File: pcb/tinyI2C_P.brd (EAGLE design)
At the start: 83.2 x 83.2 mm, 226 parts, among them IC1 74ABT125BQ, IC10 74ABT125BQ, IC11 TPS76318, IC12 74ABT125BQ, IC13 TPS76318, IC14 74ABT125BQ, IC15 TPS76318, IC16 74ABT125BQ, IC2 TPS76318, IC3 TPS76318, IC4 74ABT125BQ, IC5 TPS76318, IC6 74ABT125BQ, IC7 TPS76318, IC8 74ABT125BQ, IC9 TPS76318, U1 LPC824M201JHI33, U2 LPC824M201JHI33, U3 LPC824M201JHI33, U4 LPC824M201JHI33, U5 LPC824M201JHI33, U6 LPC824M201JHI33, U7 LPC824M201JHI33, U8 LPC824M201JHI33, X1 TSW-112-02-S-S, X10 TSW-112-02-S-S, X11 TSW-112-02-S-S, X12 TSW-102-02-S-S, X13 TSW-106-02-S-S-RA, X14 TSW-112-02-S-S, X15 TSW-112-02-S-S, X16 TSW-102-02-S-S, X17 TSW-106-02-S-S-RA, X18 TSW-112-02-S-S, X19 TSW-112-02-S-S, X2 TSW-106-02-S-S-RA, X20 TSW-102-02-S-S, X21 TSW-106-02-S-S-RA, X22 TSW-112-02-S-S, X23 TSW-112-02-S-S, X24 TSW-102-02-S-S, X25 TSW-106-02-S-S-RA, X26 TSW-112-02-S-S, X27 TSW-112-02-S-S, X28 TSW-102-02-S-S, X29 TSW-106-02-S-S-RA, X3 TSW-112-02-S-S, X30 TSW-112-02-S-S, X31 TSW-112-02-S-S, X32 TSW-102-02-S-S, X4 TSW-102-02-S-S, X5 TSW-106-02-S-S-RA, X6 TSW-112-02-S-S, X7 TSW-112-02-S-S, X8 TSW-102-02-S-S, X9 TSW-106-02-S-S-RA

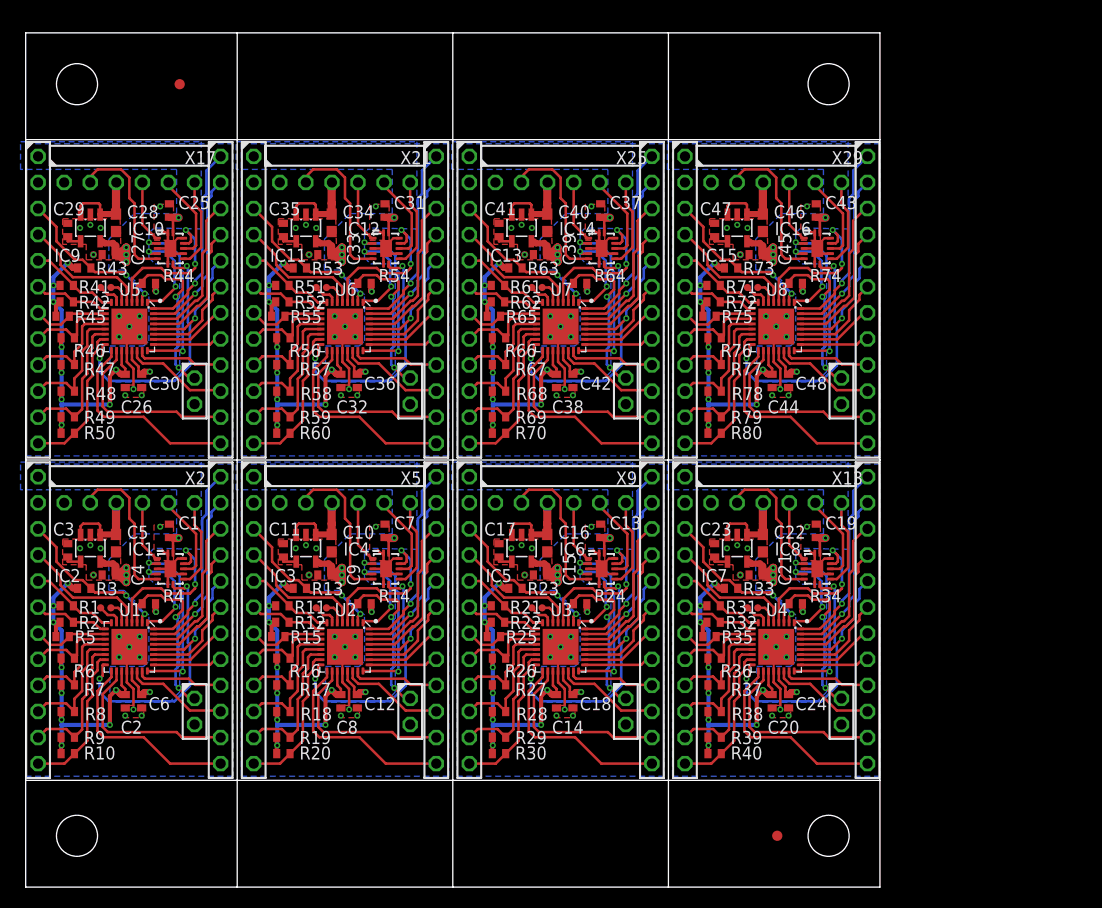
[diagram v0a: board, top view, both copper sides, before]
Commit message: [ PCB ] panelized as per update
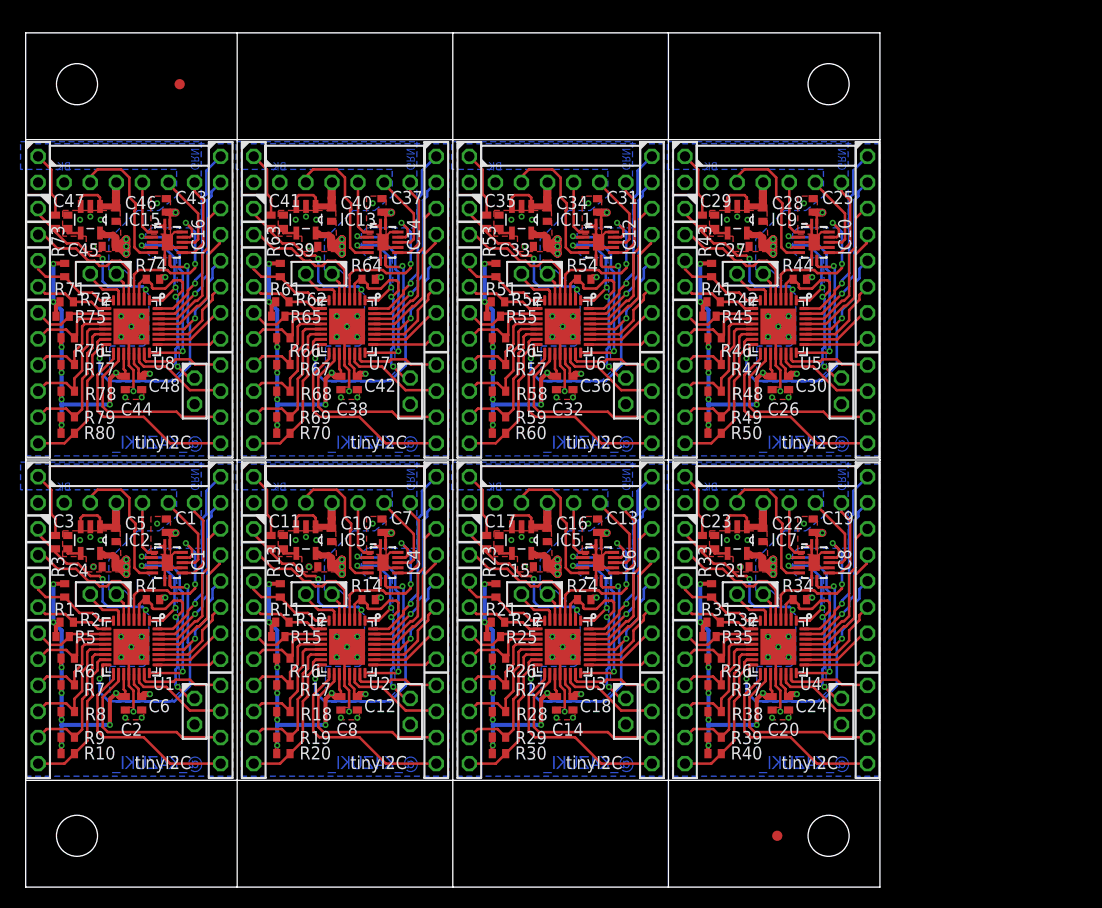
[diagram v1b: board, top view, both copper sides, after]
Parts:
- removed TP27, TP28, TP29, TP30, TP31, TP32, TP33, TP34, TP35, TP36, TP37, TP38, TP39, TP40, TP41, TP42: TPTP07R, testpad:TP07R
- added X33, X37, X38: TSW-112-02-S-S, con-samtec.local:TSW-112-02-S-S
- added X34, X35, X39, X40: TSW-102-02-S-S, con-samtec.local:TSW-102-02-S-S
- added X36: TSW-106-02-S-S-RA, con-samtec.local:TSW-106-02-S-S-RA
- C10, C16, C22, C28, C34, C40, C46, C5: device rcl:C1608 -> rcl:C0402
- IC1, IC10, IC12, IC14, IC16, IC4, IC6, IC8: value 74ABT125BQ -> IC_TTL_74_125; device 74xx-eu_local:DHVQFN14 -> mylib:DHVQFN14
- IC11, IC13, IC15, IC2, IC3, IC5, IC7, IC9: value TPS76318 -> TPS73618(0.4A); device texas:SOT23-DBV -> mylib:SOT95P280X145-5N
- U1, U2, U3, U4, U5, U6, U7, U8: device mbed-HDK:HVQFN33 -> mylib:HVQFN33
- X10, X14, X15, X19, X30: value TSW-112-02-S-S -> TSW-102-02-S-S; device con-samtec.local:TSW-112-02-S-S -> con-samtec.local:TSW-102-02-S-S
- X11, X26, X31, X6: value TSW-112-02-S-S -> TSW-106-02-S-S-RA; device con-samtec.local:TSW-112-02-S-S -> con-samtec.local:TSW-106-02-S-S-RA
- X12, X28, X32, X8: value TSW-102-02-S-S -> TSW-112-02-S-S; device con-samtec.local:TSW-102-02-S-S -> con-samtec.local:TSW-112-02-S-S
- X13, X17: value TSW-106-02-S-S-RA -> TSW-112-02-S-S; device con-samtec.local:TSW-106-02-S-S-RA -> con-samtec.local:TSW-112-02-S-S
- X16: value TSW-102-02-S-S -> TSW-106-02-S-S-RA; device con-samtec.local:TSW-102-02-S-S -> con-samtec.local:TSW-106-02-S-S-RA
- X25, X29, X5, X9: value TSW-106-02-S-S-RA -> TSW-102-02-S-S; device con-samtec.local:TSW-106-02-S-S-RA -> con-samtec.local:TSW-102-02-S-S
- moved X18 86.6 mm to (82.0, 26.0)
- moved X19 72.5 mm to (79.5, 17.1)
- moved X17 69.8 mm to (64.2, 26.0), turned to 90 degrees
- moved R73 66.0 mm to (2.90, 64.8), turned to 90 degrees
- moved R44 63.4 mm to (75.4, 59.2)
- moved IC16 63.3 mm to (13.8, 62.8)
- moved C43 63.3 mm to (13.7, 66.4)
- moved R71 63.2 mm to (3.80, 60.1), turned to 90 degrees
- moved U5 63.2 mm to (73.3, 54.6)
- moved C28 63.0 mm to (71.8, 65.5)
- moved C46 63.0 mm to (8.80, 65.5)
- moved IC15 63.0 mm to (6.30, 65.0), turned to 270 degrees
- moved IC9 63.0 mm to (69.3, 65.0), turned to 270 degrees
- moved C27 63.0 mm to (71.1, 62.4)
- moved C29 63.0 mm to (67.1, 64.8)
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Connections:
- net !ISP!1: now also X7.3; no longer X6.3
- net !ISP!2: now also X12.3; no longer X10.3
- net !ISP!3: now also X17.3; no longer X14.3
- net !ISP!4: now also X22.3; no longer X18.3
- net !ISP!5: now also X27.3; no longer X22.3
- net !ISP!6: now also X32.3; no longer X26.3
- net !ISP!7: now also X37.3; no longer X30.3
- net !RESET!1: now also X9.1; no longer X8.1
- net !RESET!2: now also X14.1; no longer X12.1
- net !RESET!3: now also X19.1; no longer X16.1
- net !RESET!4: now also X24.1; no longer X20.1
- net !RESET!5: now also X29.1; no longer X24.1
- net !RESET!6: now also X34.1; no longer X28.1
- net !RESET!7: now also X39.1; no longer X32.1
- net 1.8V1: now also X7.1; no longer X6.1
- net 1.8V2: now also TP10.TP, X12.1; no longer TP14.TP, X10.1
- net 1.8V3: now also TP13.TP, X17.1; no longer TP19.TP, X14.1
- net 1.8V4: now also TP16.TP, X22.1; no longer TP24.TP, X18.1
- net 1.8V5: now also TP19.TP, X27.1; no longer TP29.TP, X22.1
- net 1.8V6: now also TP22.TP, X32.1; no longer TP34.TP, X26.1
- net 1.8V7: now also TP25.TP, X37.1; no longer TP39.TP, X30.1
- net 5V1: now also X6.3; no longer X5.3
- net 5V2: now also TP9.TP, X11.3; no longer TP13.TP, X9.3
- net 5V3: now also TP12.TP, X16.3; no longer TP18.TP, X13.3
- net 5V4: now also TP15.TP, X21.3; no longer TP23.TP, X17.3
- net 5V5: now also TP18.TP, X26.3; no longer TP28.TP, X21.3
- net 5V6: now also TP21.TP, X31.3; no longer TP33.TP, X25.3
- net 5V7: now also TP24.TP, X36.3; no longer TP38.TP, X29.3
- net CTS<-1: now also X6.2; no longer X5.2
- net CTS<-2: now also X11.2; no longer X9.2
- net CTS<-3: now also X16.2; no longer X13.2
- net CTS<-4: now also X21.2; no longer X17.2
- net CTS<-5: now also X26.2; no longer X21.2
- net CTS<-6: now also X31.2; no longer X25.2
- net CTS<-7: now also X36.2; no longer X29.2
- net GND1: now also TP8.TP, X6.1, X7.2, X9.2; no longer TP12.TP, X5.1, X6.2, X8.2
- net GND2: now also TP11.TP, X11.1, X14.2; no longer TP17.TP, X10.2, X9.1
- net GND3: now also TP14.TP, X16.1, X17.2, X19.2; no longer TP22.TP, X13.1, X14.2, X16.2
- net GND4: now also TP17.TP, X21.1, X22.2, X24.2; no longer TP27.TP, X17.1, X18.2, X20.2
- net GND5: now also TP20.TP, X26.1, X27.2, X29.2; no longer TP32.TP, X21.1, X22.2, X24.2
- net GND6: now also TP23.TP, X31.1, X32.2, X34.2; no longer TP37.TP, X25.1, X26.2, X28.2
- net GND7: now also TP26.TP, X36.1, X37.2, X39.2; no longer TP42.TP, X29.1, X30.2, X32.2
- net GPIO08: now also X7.4; no longer X6.4
- net GPIO09: now also X7.7; no longer X6.7
- net GPIO100: now also X33.5; no longer X27.5
- net GPIO101: now also X33.4; no longer X27.4
- net GPIO102: now also X33.3; no longer X27.3
- net GPIO103: now also X33.2; no longer X27.2
- net GPIO104: now also X33.1; no longer X27.1
- net GPIO105: now also X37.4; no longer X30.4
- net GPIO106: now also X37.7; no longer X30.7
- net GPIO107: now also X37.8; no longer X30.8
- net GPIO108: now also X37.9; no longer X30.9
- net GPIO109: now also X37.10; no longer X30.10
- net GPIO110: now also X37.11; no longer X30.11
- net GPIO111: now also X37.12; no longer X30.12
- net GPIO112: now also X38.8; no longer X31.8
- net GPIO113: now also X38.7; no longer X31.7
- net GPIO114: now also X38.6; no longer X31.6
- net GPIO115: now also X38.5; no longer X31.5
- net GPIO116: now also X38.4; no longer X31.4
- net GPIO117: now also X38.3; no longer X31.3
- net GPIO118: now also X38.2; no longer X31.2
- net GPIO119: now also X38.1; no longer X31.1
- net GPIO17: now also X7.8; no longer X6.8
- net GPIO18: now also X7.9; no longer X6.9
- net GPIO19: now also X7.10; no longer X6.10
- net GPIO20: now also X7.11; no longer X6.11
- net GPIO21: now also X7.12; no longer X6.12
- net GPIO22: now also X8.8; no longer X7.8
- net GPIO23: now also X8.7; no longer X7.7
- net GPIO24: now also X8.6; no longer X7.6
- net GPIO25: now also X8.5; no longer X7.5
- net GPIO26: now also X8.4; no longer X7.4
- net GPIO27: now also X8.3; no longer X7.3
- net GPIO28: now also X8.2; no longer X7.2
- net GPIO29: now also X8.1; no longer X7.1
- net GPIO30: now also X12.4; no longer X10.4
- net GPIO31: now also X12.7; no longer X10.7
- net GPIO32: now also X12.8; no longer X10.8
- net GPIO33: now also X12.9; no longer X10.9
- net GPIO34: now also X12.10; no longer X10.10
- net GPIO35: now also X12.11; no longer X10.11
- net GPIO36: now also X12.12; no longer X10.12
- net GPIO37: now also X13.8; no longer X11.8
- net GPIO38: now also X13.7; no longer X11.7
- net GPIO39: now also X13.6; no longer X11.6
- net GPIO40: now also X13.5; no longer X11.5
- net GPIO41: now also X13.4; no longer X11.4
- net GPIO42: now also X13.3; no longer X11.3
- net GPIO43: now also X13.2; no longer X11.2
- net GPIO44: now also X13.1; no longer X11.1
- net GPIO45: now also X17.4; no longer X14.4
- net GPIO46: now also X17.7; no longer X14.7
- net GPIO47: now also X17.8; no longer X14.8
- net GPIO48: now also X17.9; no longer X14.9
- net GPIO49: now also X17.10; no longer X14.10
- net GPIO50: now also X17.11; no longer X14.11
- net GPIO51: now also X17.12; no longer X14.12
- net GPIO52: now also X18.8; no longer X15.8
- net GPIO53: now also X18.7; no longer X15.7
- net GPIO54: now also X18.6; no longer X15.6
- net GPIO55: now also X18.5; no longer X15.5
- net GPIO56: now also X18.4; no longer X15.4
- net GPIO57: now also X18.3; no longer X15.3
- net GPIO58: now also X18.2; no longer X15.2
- net GPIO59: now also X18.1; no longer X15.1
- net GPIO60: now also X22.4; no longer X18.4
- net GPIO61: now also X22.7; no longer X18.7
- net GPIO62: now also X22.8; no longer X18.8
- net GPIO63: now also X22.9; no longer X18.9
- net GPIO64: now also X22.10; no longer X18.10
- net GPIO65: now also X22.11; no longer X18.11
- net GPIO66: now also X22.12; no longer X18.12
- net GPIO67: now also X23.8; no longer X19.8
- net GPIO68: now also X23.7; no longer X19.7
- net GPIO69: now also X23.6; no longer X19.6
- net GPIO70: now also X23.5; no longer X19.5
- net GPIO71: now also X23.4; no longer X19.4
- net GPIO72: now also X23.3; no longer X19.3
- net GPIO73: now also X23.2; no longer X19.2
- net GPIO74: now also X23.1; no longer X19.1
- net GPIO75: now also X27.4; no longer X22.4
- net GPIO76: now also X27.7; no longer X22.7
- net GPIO77: now also X27.8; no longer X22.8
- net GPIO78: now also X27.9; no longer X22.9
- net GPIO79: now also X27.10; no longer X22.10
- net GPIO80: now also X27.11; no longer X22.11
- net GPIO81: now also X27.12; no longer X22.12
- net GPIO82: now also X28.8; no longer X23.8
- net GPIO83: now also X28.7; no longer X23.7
- net GPIO84: now also X28.6; no longer X23.6
- net GPIO85: now also X28.5; no longer X23.5
- net GPIO86: now also X28.4; no longer X23.4
- net GPIO87: now also X28.3; no longer X23.3
- net GPIO88: now also X28.2; no longer X23.2
- net GPIO89: now also X28.1; no longer X23.1
- net GPIO90: now also X32.4; no longer X26.4
- net GPIO91: now also X32.7; no longer X26.7
- net GPIO92: now also X32.8; no longer X26.8
- net GPIO93: now also X32.9; no longer X26.9
- net GPIO94: now also X32.10; no longer X26.10
- net GPIO95: now also X32.11; no longer X26.11
- net GPIO96: now also X32.12; no longer X26.12
- net GPIO97: now also X33.8; no longer X27.8
- net GPIO98: now also X33.7; no longer X27.7
- net GPIO99: now also X33.6; no longer X27.6
- net I2C_SCL1: now also X7.6; no longer X6.6
- net I2C_SCL2: now also X12.6; no longer X10.6
- net I2C_SCL3: now also X17.6; no longer X14.6
- net I2C_SCL4: now also X22.6; no longer X18.6
- net I2C_SCL5: now also X27.6; no longer X22.6
- net I2C_SCL6: now also X32.6; no longer X26.6
- net I2C_SCL7: now also X37.6; no longer X30.6
- net I2C_SDA1: now also X7.5; no longer X6.5
- net I2C_SDA2: now also X12.5; no longer X10.5
- net I2C_SDA3: now also X17.5; no longer X14.5
- net I2C_SDA4: now also X22.5; no longer X18.5
- net I2C_SDA5: now also X27.5; no longer X22.5
- net I2C_SDA6: now also X32.5; no longer X26.5
- net I2C_SDA7: now also X37.5; no longer X30.5
- net RTS->1: now also X6.6; no longer X5.6
- net RTS->2: now also X11.6; no longer X9.6
- net RTS->3: now also X16.6; no longer X13.6
- net RTS->4: now also X21.6; no longer X17.6
- net RTS->5: now also X26.6; no longer X21.6
- net RTS->6: now also X31.6; no longer X25.6
- net RTS->7: now also X36.6; no longer X29.6
- net RX<-1: now also X6.5; no longer X5.5
- net RX<-2: now also X11.5; no longer X9.5
- net RX<-3: now also X16.5; no longer X13.5
- net RX<-4: now also X21.5; no longer X17.5
- net RX<-5: now also X26.5; no longer X21.5
- net RX<-6: now also X31.5; no longer X25.5
- net RX<-7: now also X36.5; no longer X29.5
- net SPI_CS1: now also X8.12; no longer X7.12
- net SPI_CS2: now also X13.12; no longer X11.12
- net SPI_CS3: now also X18.12; no longer X15.12
- net SPI_CS4: now also X23.12; no longer X19.12
- net SPI_CS5: now also X28.12; no longer X23.12
- net SPI_CS6: now also X33.12; no longer X27.12
- net SPI_CS7: now also X38.12; no longer X31.12
- net SPI_MISO1: now also X8.10; no longer X7.10
- net SPI_MISO2: now also X13.10; no longer X11.10
- net SPI_MISO3: now also X18.10; no longer X15.10
- net SPI_MISO4: now also X23.10; no longer X19.10
- net SPI_MISO5: now also X28.10; no longer X23.10
- net SPI_MISO6: now also X33.10; no longer X27.10
- net SPI_MISO7: now also X38.10; no longer X31.10
- net SPI_MOSI1: now also X8.9; no longer X7.9
- net SPI_MOSI2: now also X13.9; no longer X11.9
- net SPI_MOSI3: now also X18.9; no longer X15.9
- net SPI_MOSI4: now also X23.9; no longer X19.9
- net SPI_MOSI5: now also X28.9; no longer X23.9
- net SPI_MOSI6: now also X33.9; no longer X27.9
- net SPI_MOSI7: now also X38.9; no longer X31.9
- net SPI_SCK1: now also X8.11; no longer X7.11
- net SPI_SCK2: now also X13.11; no longer X11.11
- net SPI_SCK3: now also X18.11; no longer X15.11
- net SPI_SCK4: now also X23.11; no longer X19.11
- net SPI_SCK5: now also X28.11; no longer X23.11
- net SPI_SCK6: now also X33.11; no longer X27.11
- net SPI_SCK7: now also X38.11; no longer X31.11
- net SWCLK: now also X5.1; no longer TP8.TP
- net SWCLK1: now also X10.1; no longer TP10.TP
- net SWCLK2: now also X15.1; no longer TP15.TP
- net SWCLK3: now also X20.1; no longer TP20.TP
- net SWCLK4: now also X25.1; no longer TP25.TP
- net SWCLK5: now also X30.1; no longer TP30.TP
- net SWCLK6: now also X35.1; no longer TP35.TP
- net SWCLK7: now also X40.1; no longer TP40.TP
- net SWDIO: now also X5.2; no longer TP9.TP
- net SWDIO1: now also X10.2; no longer TP11.TP
- net SWDIO2: now also X15.2; no longer TP16.TP
- net SWDIO3: now also X20.2; no longer TP21.TP
- net SWDIO4: now also X25.2; no longer TP26.TP
- net SWDIO5: now also X30.2; no longer TP31.TP
- net SWDIO6: now also X35.2; no longer TP36.TP
- net SWDIO7: now also X40.2; no longer TP41.TP
- net TX->1: now also X6.4; no longer X5.4
- net TX->2: now also X11.4; no longer X9.4
- net TX->3: now also X16.4; no longer X13.4
- net TX->4: now also X21.4; no longer X17.4
- net TX->5: now also X26.4; no longer X21.4
- net TX->6: now also X31.4; no longer X25.4
- net TX->7: now also X36.4; no longer X29.4
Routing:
- net 1.8V6: track 50.1 -> 53.9 mm, vias 15 -> 14
- net 1.8V7: track 50.1 -> 53.9 mm, vias 15 -> 14
- net 1.8V5: track 50.1 -> 53.9 mm, vias 15 -> 14
- net 1.8V4: track 50.1 -> 53.9 mm, vias 15 -> 14
- net 1.8V2: track 50.1 -> 53.9 mm, vias 15 -> 14
- net 1.8V3: track 50.1 -> 53.9 mm, vias 15 -> 14
- net 1.8V: track 50.1 -> 53.9 mm, vias 15 -> 14
- net 1.8V1: track 50.1 -> 53.9 mm, vias 15 -> 14
- net SWDIO7: track 2.44 -> 4.45 mm
- net SWDIO6: track 2.44 -> 4.45 mm
- net SWDIO5: track 2.44 -> 4.45 mm
- net SWDIO4: track 2.44 -> 4.45 mm
- net SWDIO: track 2.44 -> 4.45 mm
- net SWDIO1: track 2.44 -> 4.45 mm
- net SWDIO3: track 2.44 -> 4.45 mm
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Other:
- board text added: "@_K4ZUKI_"
- board text added: "BK"
- board text added: "GRN"
- board text added: "tinyI2C"
- board text removed: "X2"

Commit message: [ PCB ] trace change and panelize
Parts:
- moved R16 0.50 mm to (24.6, 22.3)
- moved R17 0.50 mm to (24.6, 19.7)
- moved R18 0.50 mm to (24.6, 17.1)
- moved R19 0.50 mm to (24.6, 14.6)
- moved R26 0.50 mm to (45.6, 22.3)
- moved R27 0.50 mm to (45.6, 19.7)
- moved R28 0.50 mm to (45.6, 17.1)
- moved R29 0.50 mm to (45.6, 14.6)
- moved R36 0.50 mm to (66.6, 22.3)
- moved R37 0.50 mm to (66.6, 19.7)
- moved R38 0.50 mm to (66.6, 17.1)
- moved R39 0.50 mm to (66.6, 14.6)
- moved R46 0.50 mm to (66.6, 53.5)
- moved R47 0.50 mm to (66.6, 50.9)
- moved R48 0.50 mm to (66.6, 48.3)
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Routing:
- net 1.8V7: track 53.9 -> 54.7 mm
- net 1.8V6: track 53.9 -> 54.7 mm
- net 1.8V4: track 53.9 -> 54.7 mm
- net 1.8V5: track 53.9 -> 54.7 mm
- net 1.8V3: track 53.9 -> 54.7 mm
- net 1.8V2: track 53.9 -> 54.7 mm
- net 1.8V1: track 53.9 -> 54.7 mm
- net 1.8V: track 53.9 -> 54.7 mm

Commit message: [ PCB ] panelized based on sch/brd updates
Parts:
- added C49, C50, C51, C52, C53, C54, C55, C56, C57, C58, C59, C60, C61, C62, C63, C64, C65, C66, C67, C68, C69, C70, C71, C72: 1005, mylib:C0402
- added IC17, IC19, IC20, IC22, IC23: 74LVC1G125DCK, 74xx-little-us_local:SC70-5
- added IC18, IC21, IC24: IC_LDO_MIC5355, mylib:IC_08_0.65_160MIL
- added Q1, Q2, Q3, Q4, Q5, Q6, Q7, Q8: (no value), adafruit (1):NX3225
- added TP27, TP28, TP29, TP30, TP31, TP32, TP33, TP34: TPTP07R, testpad_local:TP07R
- added X41, X42, X46, X47, X48: TSW-102-02-S-S, con-samtec.local:TSW-102-02-S-S
- added X43: TSW-106-02-S-S-RA, con-samtec.local:TSW-106-02-S-S-RA
- added X44, X45: TSW-112-02-S-S, con-samtec.local:TSW-112-02-S-S
- C1, C11, C12, C13, C14, C15, C17, C18, C19, C2, C20, C21, C23, C24, C25, C26, C27, C29, C3, C30, C31, C32, C33, C35, C36, C37, C38, C39, C4, C41, C42, C43, C44, C45, C47, C48, C6, C7, C8, C9: device rcl:C1005 -> mylib:C0402
- C10, C16, C22, C28, C34, C40, C46, C5: value 1608 -> 1005; device rcl:C0402 -> mylib:C0402
- IC1, IC10, IC14, IC16, IC4, IC8: value IC_TTL_74_125 -> 74LVC1G125DCK; device mylib:DHVQFN14 -> 74xx-little-us_local:SC70-5
- IC11, IC13, IC2, IC5, IC7: value TPS73618(0.4A) -> 74LVC1G125DCK; device mylib:SOT95P280X145-5N -> 74xx-little-us_local:SC70-5
- IC12, IC6: value IC_TTL_74_125 -> IC_LDO_MIC5355; device mylib:DHVQFN14 -> mylib:IC_08_0.65_160MIL
- IC15, IC3, IC9: value TPS73618(0.4A) -> IC_LDO_MIC5355; device mylib:SOT95P280X145-5N -> mylib:IC_08_0.65_160MIL
- R1, R10, R11, R12, R13, R14, R15, R16, R17, R18, R19, R2, R20, R21, R22, R23, R24, R25, R26, R27, R28, R29, R3, R30, R31, R32, R33, R34, R35, R36, R37, R38, R39, R4, R40, R41, R42, R43, R44, R45, R46, R47, R48, R49, R5, R50, R51, R52, R53, R54, R55, R56, R57, R58, R59, R6, R60, R61, R62, R63, R64, R65, R66, R67, R68, R69, R7, R70, R71, R72, R73, R74, R75, R76, R77, R78, R79, R8, R80, R9: device rcl:R1005 -> mylib:C0402
- TP1, TP10, TP11, TP12, TP13, TP14, TP15, TP16, TP17, TP18, TP19, TP2, TP20, TP21, TP22, TP23, TP24, TP25, TP26, TP3, TP6, TP7, TP8, TP9: device testpad:TP07R -> testpad_local:TP07R
- X11, X16, X36, X6: value TSW-106-02-S-S-RA -> TSW-102-02-S-S; device con-samtec.local:TSW-106-02-S-S-RA -> con-samtec.local:TSW-102-02-S-S
- X12, X17, X18, X22, X23, X28: value TSW-112-02-S-S -> TSW-102-02-S-S; device con-samtec.local:TSW-112-02-S-S -> con-samtec.local:TSW-102-02-S-S
- X13, X3, X37, X7: value TSW-112-02-S-S -> TSW-106-02-S-S-RA; device con-samtec.local:TSW-112-02-S-S -> con-samtec.local:TSW-106-02-S-S-RA
- X14, X15, X20, X39, X9: value TSW-102-02-S-S -> TSW-112-02-S-S; device con-samtec.local:TSW-102-02-S-S -> con-samtec.local:TSW-112-02-S-S
- X19, X25: value TSW-102-02-S-S -> TSW-106-02-S-S-RA; device con-samtec.local:TSW-102-02-S-S -> con-samtec.local:TSW-106-02-S-S-RA
- X2, X21, X26: value TSW-106-02-S-S-RA -> TSW-112-02-S-S; device con-samtec.local:TSW-106-02-S-S-RA -> con-samtec.local:TSW-112-02-S-S
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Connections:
- removed net CTS<-: IC1.6, X2.2
- removed net CTS<-1: IC4.6, X6.2
- removed net CTS<-2: IC6.6, X11.2
- removed net CTS<-3: IC8.6, X16.2
- removed net CTS<-4: IC10.6, X21.2
- removed net CTS<-5: IC12.6, X26.2
- removed net CTS<-6: IC14.6, X31.2
- removed net CTS<-7: IC16.6, X36.2
- removed net RTS->: IC1.9, X2.6
- removed net RTS->1: IC4.9, X6.6
- removed net RTS->2: IC6.9, X11.6
- removed net RTS->3: IC8.9, X16.6
- removed net RTS->4: IC10.9, X21.6
- removed net RTS->5: IC12.9, X26.6
- removed net RTS->6: IC14.9, X31.6
- removed net RTS->7: IC16.9, X36.6
- removed net TGT_CTS: IC1.8, U1.16
- removed net TGT_CTS1: IC4.8, U2.16
- removed net TGT_CTS2: IC6.8, U3.16
- removed net TGT_CTS3: IC8.8, U4.16
- removed net TGT_CTS4: IC10.8, U5.16
- removed net TGT_CTS5: IC12.8, U6.16
- removed net TGT_CTS6: IC14.8, U7.16
- removed net TGT_CTS7: IC16.8, U8.16
- removed net TGT_RTS: IC1.5, U1.1
- removed net TGT_RTS1: IC4.5, U2.1
- removed net TGT_RTS2: IC6.5, U3.1
- removed net TGT_RTS3: IC8.5, U4.1
- removed net TGT_RTS4: IC10.5, U5.1
- removed net TGT_RTS5: IC12.5, U6.1
- removed net TGT_RTS6: IC14.5, U7.1
- removed net TGT_RTS7: IC16.5, U8.1
- new net 3.3V: C3.1, C7.1, IC1.5, IC3.8, TP6.TP
- new net 3.3V1: C14.1, C16.1, IC4.5, IC6.8, TP10.TP
- new net 3.3V2: C23.1, C25.1, IC7.5, IC9.8, TP14.TP
- new net 3.3V3: C32.1, C34.1, IC10.5, IC12.8, TP18.TP
- new net 3.3V4: C41.1, C43.1, IC13.5, IC15.8, TP22.TP
- new net 3.3V5: C50.1, C52.1, IC16.5, IC18.8, TP26.TP
- new net 3.3V6: C59.1, C61.1, IC19.5, IC21.8, TP30.TP
- new net 3.3V7: C68.1, C70.1, IC22.5, IC24.8, TP34.TP
- new net N$10: C45.1, Q5.3, U5.18
- new net N$11: C53.1, Q6.1, U6.17
- new net N$12: C54.1, Q6.3, U6.18
- new net N$13: C62.1, Q7.1, U7.17
- new net N$14: C63.1, Q7.3, U7.18
- new net N$15: C71.1, Q8.1, U8.17
- new net N$16: C72.1, Q8.3, U8.18
- new net N$9: C44.1, Q5.1, U5.17
- net !ISP!: now also X6.1; no longer X1.3
- net !ISP!1: now also X12.1; no longer X7.3
- net !ISP!2: now also X18.1; no longer X12.3
- net !ISP!3: now also X24.1; no longer X17.3
- net !ISP!4: now also X30.1; no longer X22.3
- net !ISP!5: now also X36.1; no longer X27.3
- net !ISP!6: now also X42.1; no longer X32.3
- net !ISP!7: now also X48.1; no longer X37.3
- net !RESET!1: now also X10.1; no longer X9.1
- net !RESET!2: now also X16.1; no longer X14.1
- net !RESET!3: now also X22.1; no longer X19.1
- net !RESET!4: now also X28.1; no longer X24.1
- net !RESET!5: now also X34.1; no longer X29.1
- net !RESET!6: now also X40.1; no longer X34.1
- net !RESET!7: now also X46.1; no longer X39.1
- net 1.8V: now also IC3.7; no longer IC1.14
- net 1.8V1: now also C10.1, C11.1, C15.1, IC5.5, IC6.7, TP8.TP, X8.1; no longer C7.1, C8.1, C9.1, IC3.5, IC4.14, TP7.TP, X7.1
- net 1.8V2: now also C19.1, C20.1, C21.1, C24.1, IC8.5, IC9.7, TP12.TP, X14.1; no longer C13.1, C14.1, C15.1, C18.1, IC5.5, IC6.14, TP10.TP, X12.1
- net 1.8V3: now also C28.1, C29.1, C30.1, C33.1, IC11.5, IC12.7, TP16.TP, X20.1; no longer C19.1, C20.1, C21.1, C24.1, IC7.5, IC8.14, TP13.TP, X17.1
- net 1.8V4: now also C37.1, C38.1, C39.1, C42.1, IC14.5, IC15.7, TP20.TP, X26.1; no longer C25.1, C26.1, C27.1, C30.1, IC10.14, IC9.5, TP16.TP, X22.1
- net 1.8V5: now also C46.1, C47.1, C48.1, C51.1, IC17.5, IC18.7, TP24.TP, X32.1; no longer C31.1, C32.1, C33.1, C36.1, IC11.5, IC12.14, TP19.TP, X27.1
- net 1.8V6: now also C55.1, C56.1, C57.1, C60.1, IC20.5, IC21.7, TP28.TP, X38.1; no longer C37.1, C38.1, C39.1, C42.1, IC13.5, IC14.14, TP22.TP, X32.1
- net 1.8V7: now also C64.1, C65.1, C66.1, C69.1, IC23.5, IC24.7, TP32.TP, X44.1; no longer C43.1, C44.1, C45.1, C48.1, IC15.5, IC16.14, TP25.TP, X37.1
- net 5V: now also IC3.1, IC3.4, IC3.5, X1.3, X3.3; no longer IC2.1, IC2.3, X2.3
- net 5V1: now also C13.1, IC6.1, IC6.4, IC6.5, TP7.TP, X7.3, X8.3; no longer C10.1, IC3.1, IC3.3, TP6.TP, X6.3
- net 5V2: now also C22.1, IC9.1, IC9.4, IC9.5, TP11.TP, X13.3, X14.3; no longer C16.1, IC5.1, IC5.3, TP9.TP, X11.3
- net 5V3: now also C31.1, IC12.1, IC12.4, IC12.5, TP15.TP, X19.3, X20.3; no longer C22.1, IC7.1, IC7.3, TP12.TP, X16.3
- net 5V4: now also C40.1, IC15.1, IC15.4, IC15.5, TP19.TP, X25.3, X26.3; no longer C28.1, IC9.1, IC9.3, TP15.TP, X21.3
- net 5V5: now also C49.1, IC18.1, IC18.4, IC18.5, TP23.TP, X31.3, X32.3; no longer C34.1, IC11.1, IC11.3, TP18.TP, X26.3
- net 5V6: now also C58.1, IC21.1, IC21.4, IC21.5, TP27.TP, X37.3, X38.3; no longer C40.1, IC13.1, IC13.3, TP21.TP, X31.3
- net 5V7: now also C67.1, IC24.1, IC24.4, IC24.5, TP31.TP, X43.3, X44.3; no longer C46.1, IC15.1, IC15.3, TP24.TP, X36.3
- net GND: now also C7.2, C8.2, C9.2, IC1.3, IC2.1, IC2.3, IC3.2, IC3.EXP, Q1.2, Q1.4, X3.1, X6.2; no longer IC1.10, IC1.13, IC1.4, IC1.7, IC1.EXP, IC2.2, X2.1
- net GND1: now also C13.2, C14.2, C15.2, C16.2, C17.2, C18.2, IC4.3, IC5.1, IC5.3, IC6.2, IC6.EXP, Q2.2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; no longer C7.2, C8.2, C9.2, IC3.2, IC4.10, IC4.13, IC4.4, IC4.7, IC4.EXP, TP8.TP, X6.1, X7.2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
- net GND2: now also C19.2, C20.2, C21.2, C22.2, C23.2, C24.2, C25.2, C26.2, C27.2, IC7.1, IC7.3, IC8.1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; no longer C13.2, C14.2, C15.2, C16.2, C17.2, C18.2, IC5.2, IC6.1, IC6.10, IC6.13, IC6.4, IC6.7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
- net GND3: now also C28.2, C29.2, C30.2, C31.2, C32.2, C33.2, C34.2, C35.2, C36.2, IC10.1, IC10.3, IC11.1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; no longer C19.2, C20.2, C21.2, C22.2, C23.2, C24.2, IC7.2, IC8.1, IC8.10, IC8.13, IC8.4, IC8.7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
- net GND4: now also C37.2, C38.2, C39.2, C40.2, C41.2, C42.2, C43.2, C44.2, C45.2, IC13.1, IC13.3, IC14.1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; no longer C25.2, C26.2, C27.2, C28.2, C29.2, C30.2, IC10.1, IC10.10, IC10.13, IC10.4, IC10.7, IC10.EXP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
- net GND5: now also C46.2, C47.2, C48.2, C49.2, C50.2, C51.2, C52.2, C53.2, C54.2, IC16.1, IC16.3, IC17.1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; no longer C31.2, C32.2, C33.2, C34.2, C35.2, C36.2, IC11.2, IC12.1, IC12.10, IC12.13, IC12.4, IC12.7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
- net GND6: now also C55.2, C56.2, C57.2, C58.2, C59.2, C60.2, C61.2, C62.2, C63.2, IC19.1, IC19.3, IC20.1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; no longer C37.2, C38.2, C39.2, C40.2, C41.2, C42.2, IC13.2, IC14.1, IC14.10, IC14.13, IC14.4, IC14.7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
- net GND7: now also C64.2, C65.2, C66.2, C67.2, C68.2, C69.2, C70.2, C71.2, C72.2, IC22.1, IC22.3, IC23.1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; no longer C43.2, C44.2, C45.2, C46.2, C47.2, C48.2, IC15.2, IC16.1, IC16.10, IC16.13, IC16.4, IC16.7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
- net GPIO00: now also X2.1; no longer X3.1
- net GPIO01: now also X2.2; no longer X3.2
- net GPIO02: now also X2.3; no longer X3.3
- net GPIO03: now also X2.4; no longer X3.4
- net GPIO04: now also X2.5; no longer X3.5
- net GPIO05: now also X2.6; no longer X3.6
- net GPIO06: now also X2.7; no longer X3.7
- net GPIO07: now also X2.8; no longer X3.8
- net GPIO08: now also X8.4; no longer X7.4
- net GPIO09: now also X8.7; no longer X7.7
- net GPIO100: now also X39.5; no longer X33.5
- net GPIO101: now also X39.4; no longer X33.4
- net GPIO102: now also X39.3; no longer X33.3
- net GPIO103: now also X39.2; no longer X33.2
- net GPIO104: now also X39.1; no longer X33.1
- net GPIO105: now also X44.4; no longer X37.4
- net GPIO106: now also X44.7; no longer X37.7
- net GPIO107: now also X44.8; no longer X37.8
- net GPIO108: now also X44.9; no longer X37.9
- net GPIO109: now also X44.10; no longer X37.10
- net GPIO110: now also X44.11; no longer X37.11
- net GPIO111: now also X44.12; no longer X37.12
- net GPIO112: now also X45.8; no longer X38.8
- net GPIO113: now also X45.7; no longer X38.7
- net GPIO114: now also X45.6; no longer X38.6
- net GPIO115: now also X45.5; no longer X38.5
- net GPIO116: now also X45.4; no longer X38.4
- net GPIO117: now also X45.3; no longer X38.3
- net GPIO118: now also X45.2; no longer X38.2
- net GPIO119: now also X45.1; no longer X38.1
- net GPIO17: now also X8.8; no longer X7.8
- net GPIO18: now also X8.9; no longer X7.9
- net GPIO19: now also X8.10; no longer X7.10
- net GPIO20: now also X8.11; no longer X7.11
- net GPIO21: now also X8.12; no longer X7.12
- net GPIO22: now also X9.8; no longer X8.8
- net GPIO23: now also X9.7; no longer X8.7
- net GPIO24: now also X9.6; no longer X8.6
- net GPIO25: now also X9.5; no longer X8.5
- net GPIO26: now also X9.4; no longer X8.4
- net GPIO27: now also X9.3; no longer X8.3
- net GPIO28: now also X9.2; no longer X8.2
- net GPIO29: now also X9.1; no longer X8.1
- net GPIO30: now also X14.4; no longer X12.4
- net GPIO31: now also X14.7; no longer X12.7
- net GPIO32: now also X14.8; no longer X12.8
- net GPIO33: now also X14.9; no longer X12.9
- net GPIO34: now also X14.10; no longer X12.10
- net GPIO35: now also X14.11; no longer X12.11
- net GPIO36: now also X14.12; no longer X12.12
- net GPIO37: now also X15.8; no longer X13.8
- net GPIO38: now also X15.7; no longer X13.7
- net GPIO39: now also X15.6; no longer X13.6
- net GPIO40: now also X15.5; no longer X13.5
- net GPIO41: now also X15.4; no longer X13.4
- net GPIO42: now also X15.3; no longer X13.3
- net GPIO43: now also X15.2; no longer X13.2
- net GPIO44: now also X15.1; no longer X13.1
- net GPIO45: now also X20.4; no longer X17.4
- net GPIO46: now also X20.7; no longer X17.7
- net GPIO47: now also X20.8; no longer X17.8
- net GPIO48: now also X20.9; no longer X17.9
- net GPIO49: now also X20.10; no longer X17.10
- net GPIO50: now also X20.11; no longer X17.11
- net GPIO51: now also X20.12; no longer X17.12
- net GPIO52: now also X21.8; no longer X18.8
- net GPIO53: now also X21.7; no longer X18.7
- net GPIO54: now also X21.6; no longer X18.6
- net GPIO55: now also X21.5; no longer X18.5
- net GPIO56: now also X21.4; no longer X18.4
- net GPIO57: now also X21.3; no longer X18.3
- net GPIO58: now also X21.2; no longer X18.2
- net GPIO59: now also X21.1; no longer X18.1
- net GPIO60: now also X26.4; no longer X22.4
- net GPIO61: now also X26.7; no longer X22.7
- net GPIO62: now also X26.8; no longer X22.8
- net GPIO63: now also X26.9; no longer X22.9
- net GPIO64: now also X26.10; no longer X22.10
- net GPIO65: now also X26.11; no longer X22.11
- net GPIO66: now also X26.12; no longer X22.12
- net GPIO67: now also X27.8; no longer X23.8
- net GPIO68: now also X27.7; no longer X23.7
- net GPIO69: now also X27.6; no longer X23.6
- net GPIO70: now also X27.5; no longer X23.5
- net GPIO71: now also X27.4; no longer X23.4
- net GPIO72: now also X27.3; no longer X23.3
- net GPIO73: now also X27.2; no longer X23.2
- net GPIO74: now also X27.1; no longer X23.1
- net GPIO75: now also X32.4; no longer X27.4
- net GPIO76: now also X32.7; no longer X27.7
- net GPIO77: now also X32.8; no longer X27.8
- net GPIO78: now also X32.9; no longer X27.9
- net GPIO79: now also X32.10; no longer X27.10
- net GPIO80: now also X32.11; no longer X27.11
- net GPIO81: now also X32.12; no longer X27.12
- net GPIO82: now also X33.8; no longer X28.8
- net GPIO83: now also X33.7; no longer X28.7
- net GPIO84: now also X33.6; no longer X28.6
- net GPIO85: now also X33.5; no longer X28.5
- net GPIO86: now also X33.4; no longer X28.4
- net GPIO87: now also X33.3; no longer X28.3
- net GPIO88: now also X33.2; no longer X28.2
- net GPIO89: now also X33.1; no longer X28.1
- net GPIO90: now also X38.4; no longer X32.4
- net GPIO91: now also X38.7; no longer X32.7
- net GPIO92: now also X38.8; no longer X32.8
- net GPIO93: now also X38.9; no longer X32.9
- net GPIO94: now also X38.10; no longer X32.10
- net GPIO95: now also X38.11; no longer X32.11
- net GPIO96: now also X38.12; no longer X32.12
- net GPIO97: now also X39.8; no longer X33.8
- net GPIO98: now also X39.7; no longer X33.7
- net GPIO99: now also X39.6; no longer X33.6
- net I2C_SCL1: now also X8.6; no longer X7.6
- net I2C_SCL2: now also X14.6; no longer X12.6
- net I2C_SCL3: now also X20.6; no longer X17.6
- net I2C_SCL4: now also X26.6; no longer X22.6
- net I2C_SCL5: now also X32.6; no longer X27.6
- net I2C_SCL6: now also X38.6; no longer X32.6
- net I2C_SCL7: now also X44.6; no longer X37.6
- net I2C_SDA1: now also X8.5; no longer X7.5
- net I2C_SDA2: now also X14.5; no longer X12.5
- net I2C_SDA3: now also X20.5; no longer X17.5
- net I2C_SDA4: now also X26.5; no longer X22.5
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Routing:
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- added copper zone on layer 1, net 1.8V
- added copper zone on layer 1, net 1.8V1
- added copper zone on layer 1, net 1.8V2
- added copper zone on layer 1, net 1.8V3
- added copper zone on layer 1, net 1.8V4
- added copper zone on layer 1, net 1.8V5
- added copper zone on layer 1, net 1.8V6
- added copper zone on layer 1, net 1.8V7
- added copper zone on layer 1, net 3.3V
- added copper zone on layer 1, net 3.3V1
- added copper zone on layer 1, net 3.3V2
- added copper zone on layer 1, net 3.3V3
- added copper zone on layer 1, net 3.3V4
- added copper zone on layer 1, net 3.3V5
- added copper zone on layer 1, net 3.3V6
- added copper zone on layer 1, net 3.3V7
- added copper zone on layer 1, net 5V
- added copper zone on layer 1, net 5V1
- added copper zone on layer 1, net 5V2
- added copper zone on layer 1, net 5V3
- added copper zone on layer 1, net 5V4
- added copper zone on layer 1, net 5V5
- added copper zone on layer 1, net 5V6
- added copper zone on layer 1, net 5V7
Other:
- board text added: "!ISP"
- board text added: "!RST"
- board text added: "C7"
- board text added: "C8"
- board text added: "C9"
- board text added: "IC3"

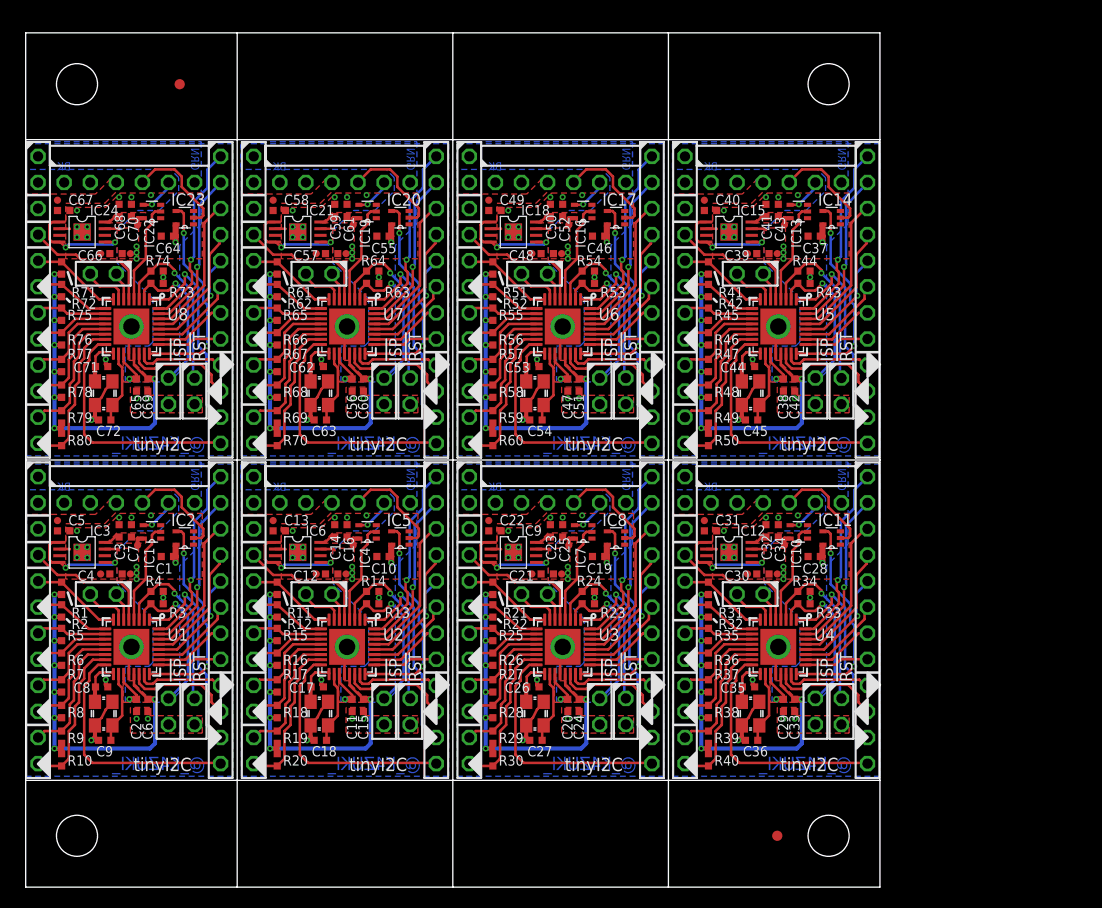
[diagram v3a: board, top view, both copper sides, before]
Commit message: [ PCB ] panelize as updated
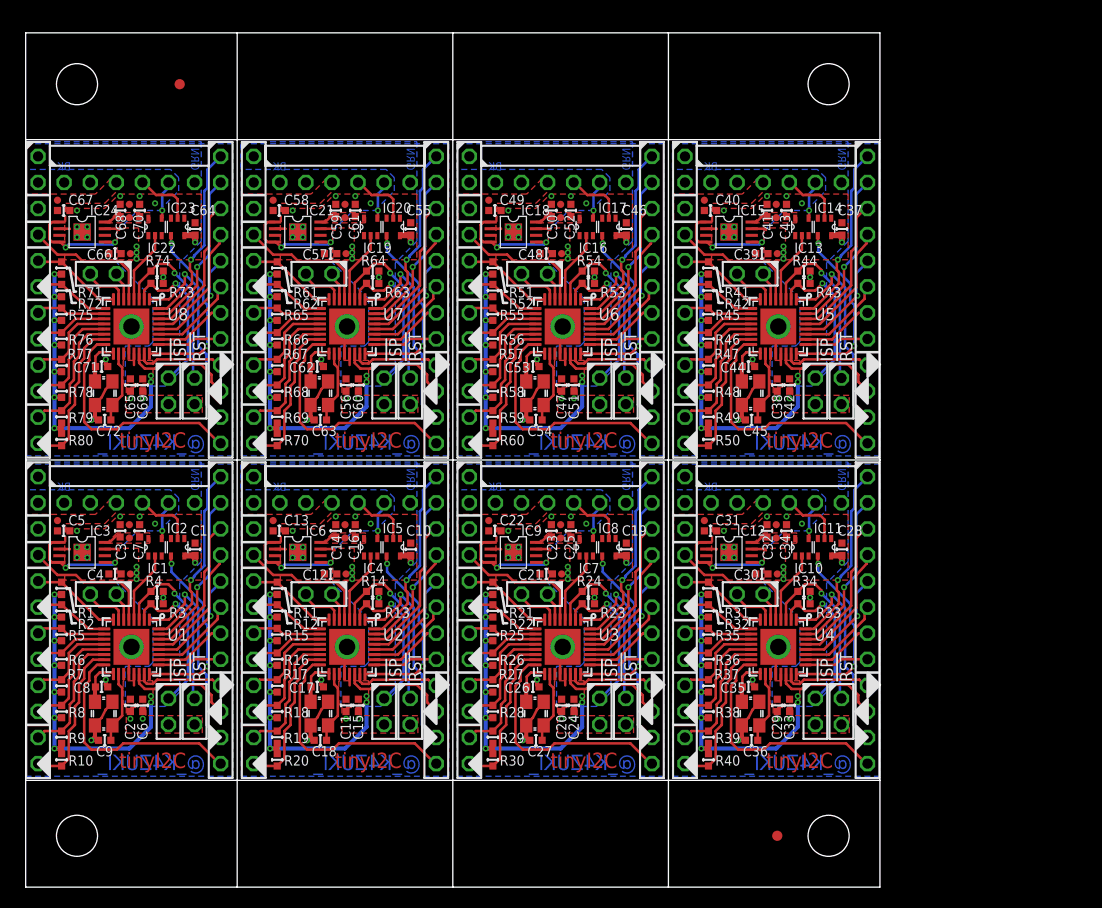
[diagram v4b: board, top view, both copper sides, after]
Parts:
- moved TP13 5.56 mm to (52.1, 35.3)
- moved TP25 5.56 mm to (52.1, 66.5)
- moved TP29 5.56 mm to (31.1, 66.5)
- moved TP3 5.56 mm to (10.1, 35.3)
- moved TP33 5.56 mm to (10.1, 66.5)
- moved TP9 5.56 mm to (31.1, 35.3)
- moved TP17 5.56 mm to (73.1, 35.3)
- moved TP21 5.56 mm to (73.1, 66.5)
- moved C10 2.79 mm to (37.5, 32.9), turned to 90 degrees
- moved C19 2.79 mm to (58.5, 32.9), turned to 90 degrees
- moved C28 2.79 mm to (79.5, 32.9), turned to 90 degrees
- moved C37 2.79 mm to (79.5, 64.1), turned to 90 degrees
- moved C46 2.79 mm to (58.5, 64.1), turned to 90 degrees
- moved C55 2.79 mm to (37.5, 64.1), turned to 90 degrees
- moved C1 2.79 mm to (16.5, 32.9), turned to 90 degrees
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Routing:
- net 1.8V2: track 47.2 -> 39.1 mm
- net 1.8V1: track 47.2 -> 39.1 mm
- net 1.8V7: track 47.2 -> 39.1 mm
- net 1.8V5: track 47.2 -> 39.1 mm
- net 1.8V: track 47.2 -> 39.1 mm
- net 1.8V6: track 47.2 -> 39.1 mm
- net 1.8V4: track 47.2 -> 39.1 mm
- net 1.8V3: track 47.2 -> 39.1 mm
- net TX->4: track 10.4 -> 5.96 mm
- net TX->7: track 10.4 -> 5.96 mm
- net TX->6: track 10.4 -> 5.96 mm
- net TX->5: track 10.4 -> 5.96 mm
- net TX->3: track 10.4 -> 5.96 mm
- net TX->2: track 10.4 -> 5.96 mm
- net TX->1: track 10.4 -> 5.96 mm
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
